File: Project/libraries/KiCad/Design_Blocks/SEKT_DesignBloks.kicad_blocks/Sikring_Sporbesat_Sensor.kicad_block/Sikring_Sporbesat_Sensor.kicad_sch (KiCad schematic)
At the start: 18 parts, among them Q1 BC857, Q2 BC847, U1 PC847

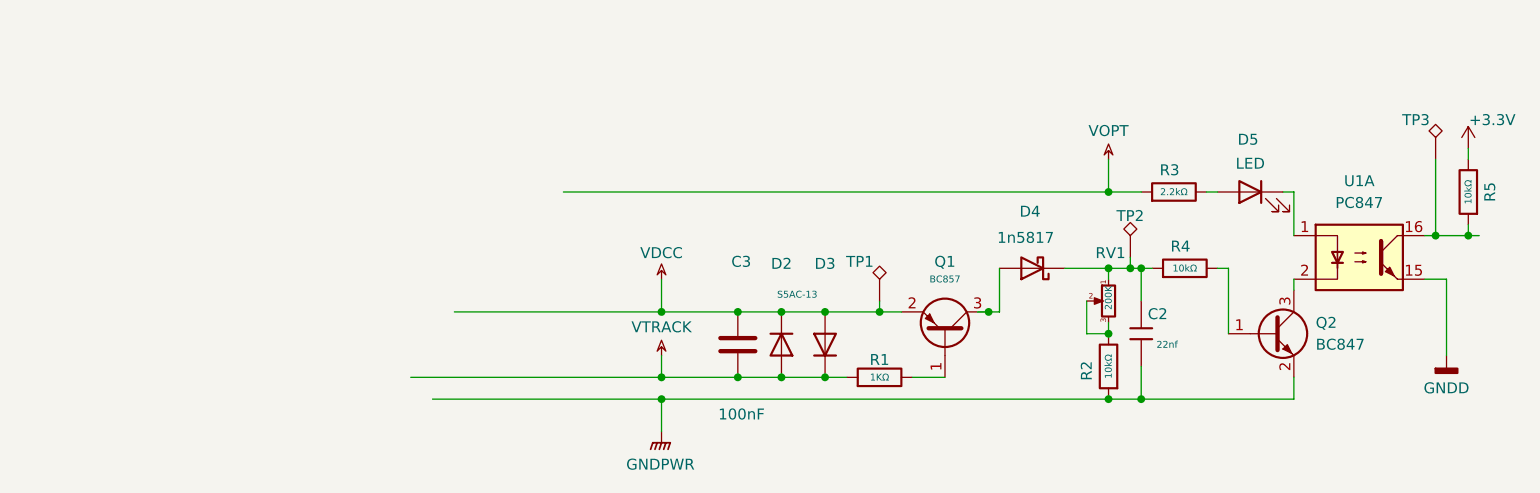
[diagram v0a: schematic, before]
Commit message: pcb på vej
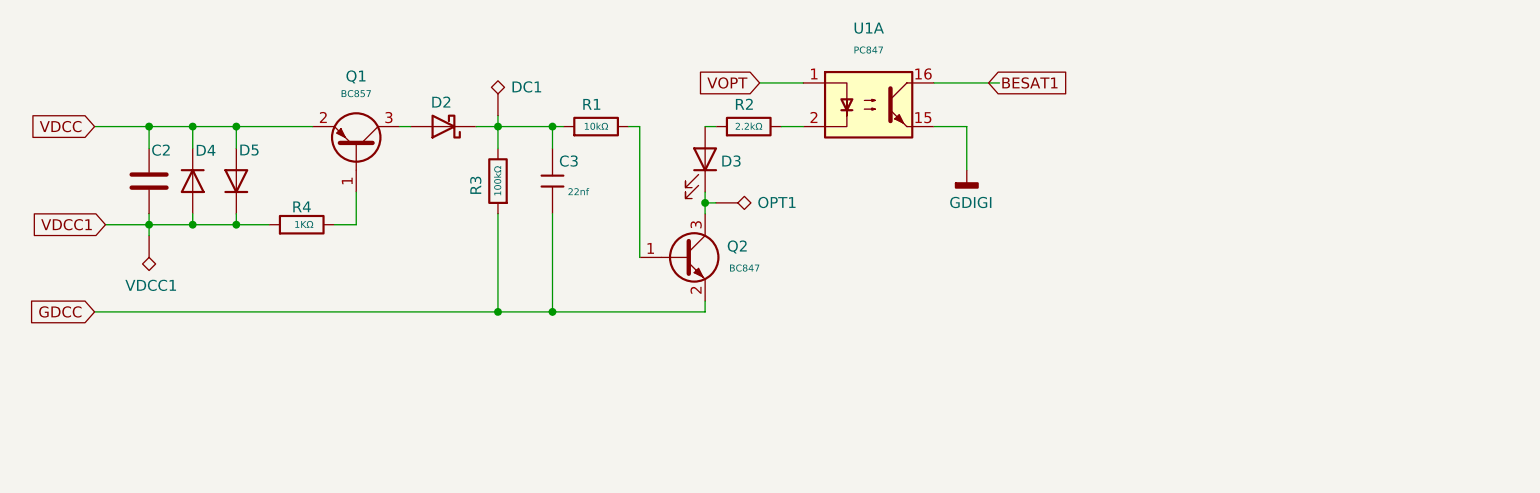
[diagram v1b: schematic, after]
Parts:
- removed D2: S5AC-13, Diode_SMD:D_MELF_Handsoldering, symbol Device:D
- removed R5: 10kΩ, PCM_JLCPCB:R_0805, symbol PCM_JLCPCB-Resistors:0805,1.8kΩ
- removed RV1: 200K, Valve:Valve_Noval_P, symbol Device:R_Potentiometer_Small
- removed TP1, TP3: Q1_Basic, TestPoint:TestPoint_Loop_D2.60mm_Drill1.4mm_Beaded, symbol Connector:TestPoint_Alt
- added D4: S5A, PCM_JLCPCB:D_SMC(DO-214AB), symbol Device:D
- added TP5: OPT1, TestPoint:TestPoint_Loop_D2.60mm_Drill1.4mm_Beaded, symbol Connector:TestPoint_Alt
- added TP6: VDCC1, TestPoint:TestPoint_Loop_D2.60mm_Drill1.4mm_Beaded, symbol Connector:TestPoint_Alt
- C2: renamed from C3; footprint (none) -> Capacitor_SMD:C_1206_3216Metric
- C3: renamed from C2; footprint PCM_JLCPCB:C_0805 -> Capacitor_SMD:C_1206_3216Metric
- D2: renamed from D4; value 1n5817 -> Schottky, SMA, 30V, 1A; footprint (none) -> PCM_JLCPCB:D_DO-214AC(SMA)
- D5: renamed from D3; value S5AC-13 -> S5A; footprint Diode_SMD:D_MELF_Handsoldering -> PCM_JLCPCB:D_SMC(DO-214AB)
- R3: renamed from R2; value 10kΩ -> 100kΩ
- TP4: renamed from TP2; value Q1_Basic -> DC1
- renumbered D5 to D3, R4 to R1, R3 to R2, R1 to R4
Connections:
- net VDCC: now also D4.1 (K)
- net VOPT: now also U1.1; no longer R2.1
- net at D3.1 (K): now also Q2.3 (C), TP5.1; no longer U1.1
- net at D3.2 (A): now also R2.1; no longer R2.2
- net at C3.1, D2.1 (K), R1.1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: now also R3.2
- net BESAT1: now reaches U1.16
- net at U1.2: now also R2.2; no longer Q2.3 (C)
- net GNDD renamed GDIGI
- net GNDPWR renamed GDCC
- net VTRACK renamed VDCC1
- net VDCC1: now also D4.2 (A), TP6.1
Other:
- moved on the sheet: C2, C3, D2, D3, D5, Q1, Q2, R1, R2, R3, R4, U1A
